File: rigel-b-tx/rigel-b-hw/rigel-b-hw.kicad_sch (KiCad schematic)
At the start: 42 parts, among them IC1 BALFHB-WL-02D3, J1 Conn_01x03_Pin, J3 Conn_01x03_Pin, U1 STM32WLE5C8Ux, U2 XC6206P332MR, U3 CH340X, U4 TYPE-C_16PIN_2MD(073), U5 X1G004131004200, U6 KH-SMA-K513-G

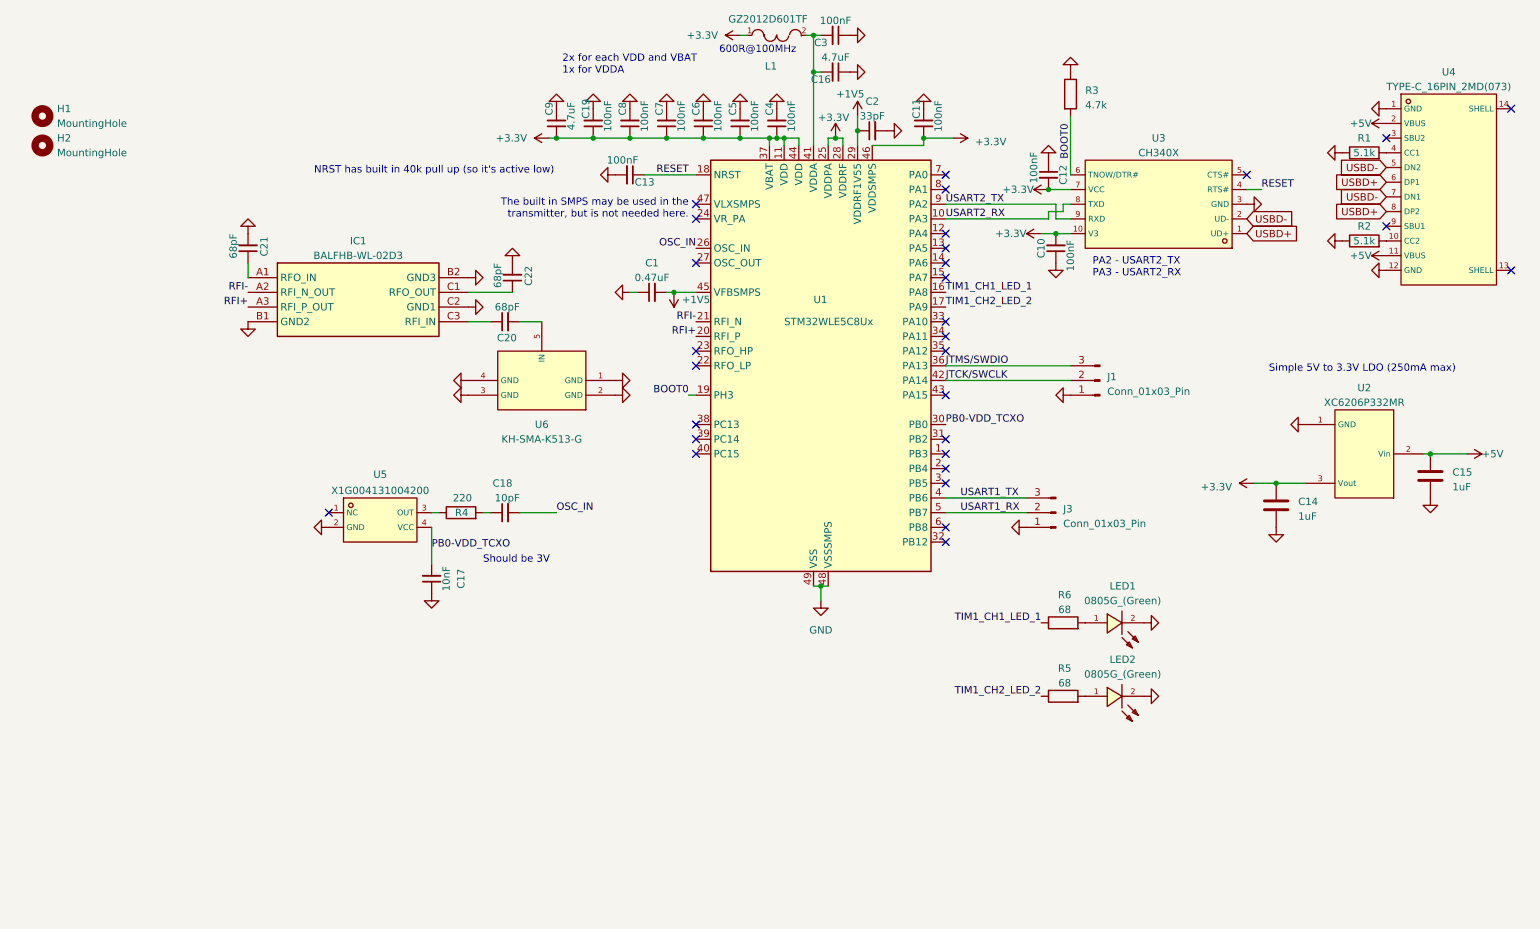
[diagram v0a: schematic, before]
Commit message: Added part of new buck converter
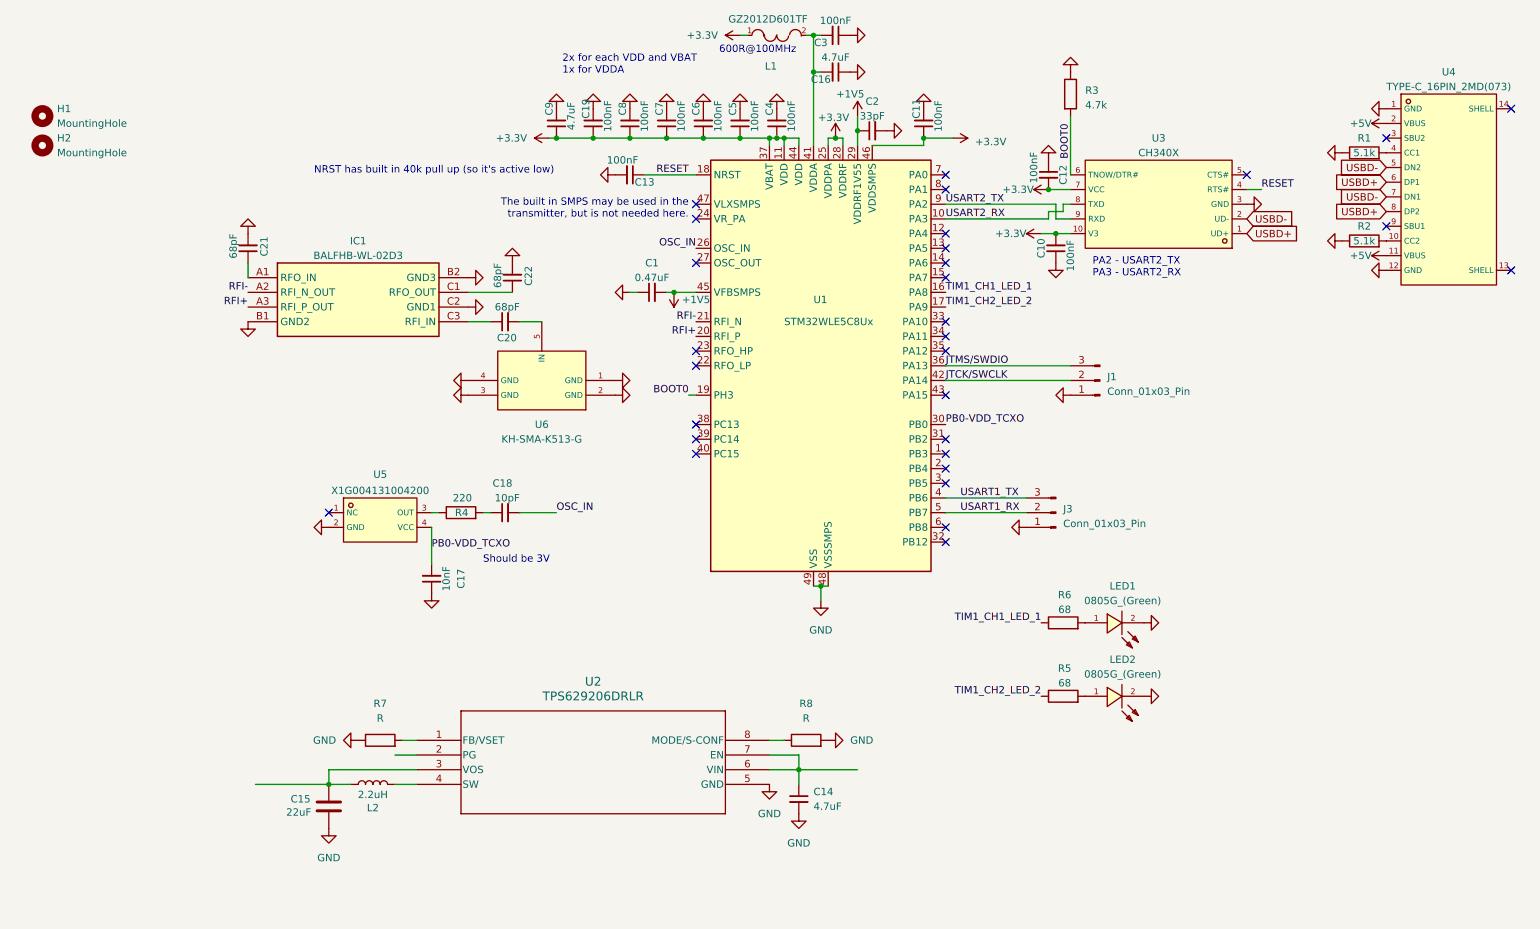
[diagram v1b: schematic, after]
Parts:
- removed C14: 1uF, Capacitor_SMD:C_0603_1608Metric, symbol Device:C
- removed U2: XC6206P332MR, jlc:SOT-23-3_L2.9-W1.6-P1.90-LS2.8-BR, symbol default_lib:XC6206P332MR
- added C14: 4.7uF, symbol Device:C_Small
- added L2: 2.2uH, symbol Device:L
- added R7, R8: R, symbol Device:R
- added U2: TPS629206DRLR, SOT5X3-8_DRL_TEX, symbol 2024-10-27_20-25-40:TPS629206DRLR
- C15: value 1uF -> 22uF; footprint Capacitor_SMD:C_0603_1608Metric -> (none)
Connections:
- net +5V: no longer C15.1
- net GND: now also C15.1, C14.2, R7.1, R8.2, U2.5 (GND); no longer C15.2
- new net: R7.2, U2.1 (FB/VSET)
- new net: C15.2, L2.1, U2.3 (VOS)
- new net: L2.2, U2.4 (SW)
- new net: C14.1, U2.6 (VIN), U2.7 (EN)
- new net: R8.1, U2.8 (MODE/S-CONF)
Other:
- note removed: "Simple 5V to 3.3V LDO (250mA max)"

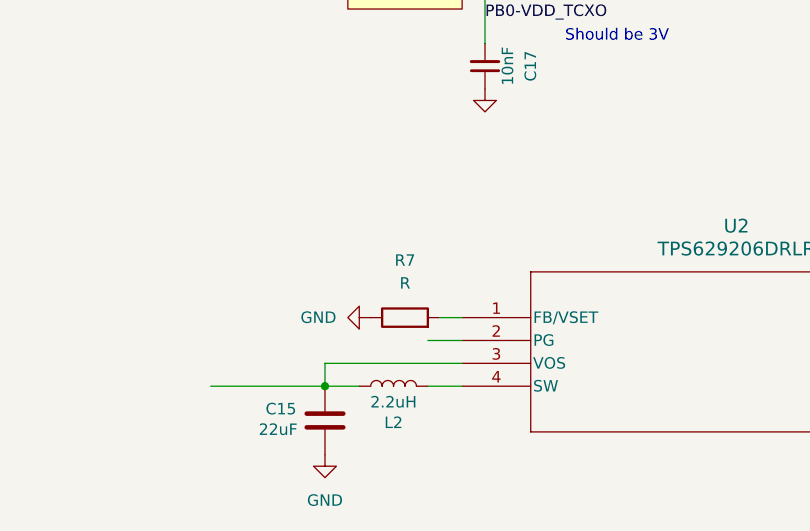
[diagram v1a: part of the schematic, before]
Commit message: Update resistor value
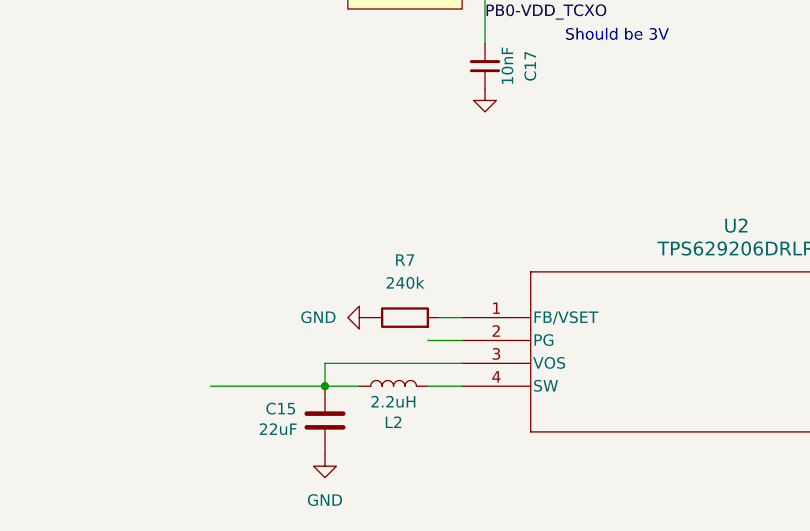
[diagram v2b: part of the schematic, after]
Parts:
- R7: value R -> 240k
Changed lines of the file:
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@@
 			)
 		)
-		(property "Value" "R"
+		(property "Value" "240k"
 			(at 83.82 134.62 90)
 			(effects

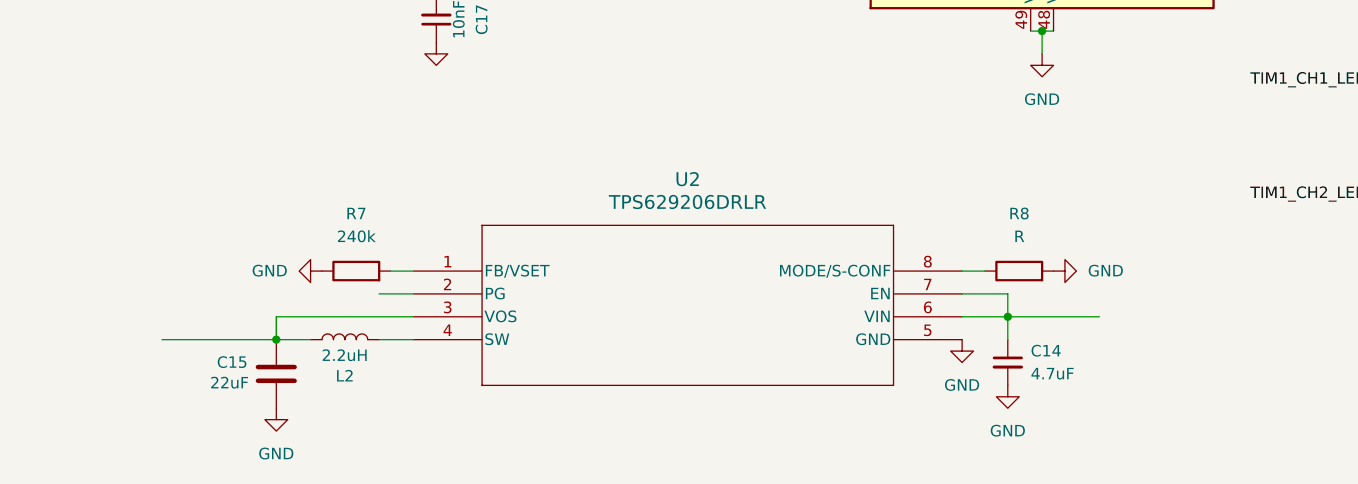
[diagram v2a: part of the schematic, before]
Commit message: Finish buck converter
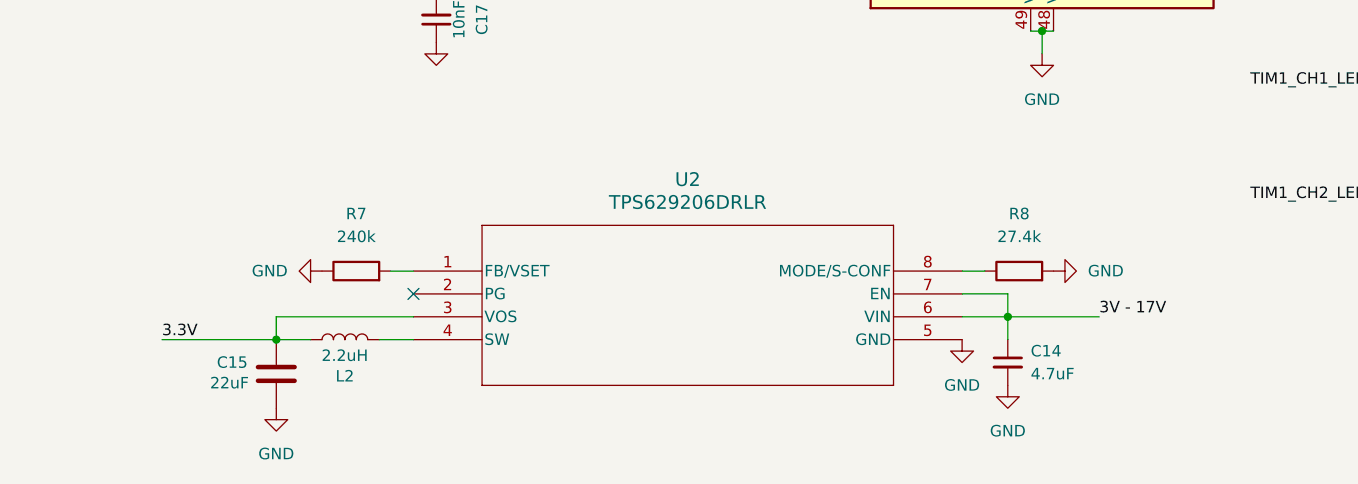
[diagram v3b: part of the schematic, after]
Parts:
- R8: value R -> 27.4k
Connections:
- net 3.3V: now reaches C15.2, L2.1, U2.3 (VOS)
- net 3V - 17V: now reaches C14.1, U2.6 (VIN), U2.7 (EN)
- no-connect marks 30 -> 31
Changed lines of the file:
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@@
+	)
+	(no_connect
+		(at 90.17 140.97)
 	)
 	(no_connect
@@
 		(pts
 			(xy 160.02 22.86) (xy 158.75 22.86)
-		)
-		(stroke
-			(width 0)
-			(type default)
-		)
-	)
-	(wire
-		(pts
-			(xy 86.36 140.97) (xy 90.17 140.97)
 		)
 		(stroke
@@
 		)
 	)
+	(label "3.3V"
+		(at 62.23 146.05 0)
+		(fields_autoplaced yes)
+		(effects
+			(font
+				(size 1.27 1.27)
+			)
+			(justify left bottom)
+		)
+	)
 	(label "JTCK{slash}SWCLK"
 		(at 181.61 76.2 0)
@@
 	(label "USART1_RX"
 		(at 184.15 99.06 0)
+		(fields_autoplaced yes)
+		(effects
+			(font
+				(size 1.27 1.27)
+			)
+			(justify left bottom)
+		)
+	)
+	(label "3V - 17V"
+		(at 166.37 143.51 0)
 		(fields_autoplaced yes)
 		(effects
@@
 			)
 		)
-		(property "Value" "R"
+		(property "Value" "27.4k"
 			(at 157.48 134.62 90)
 			(effects

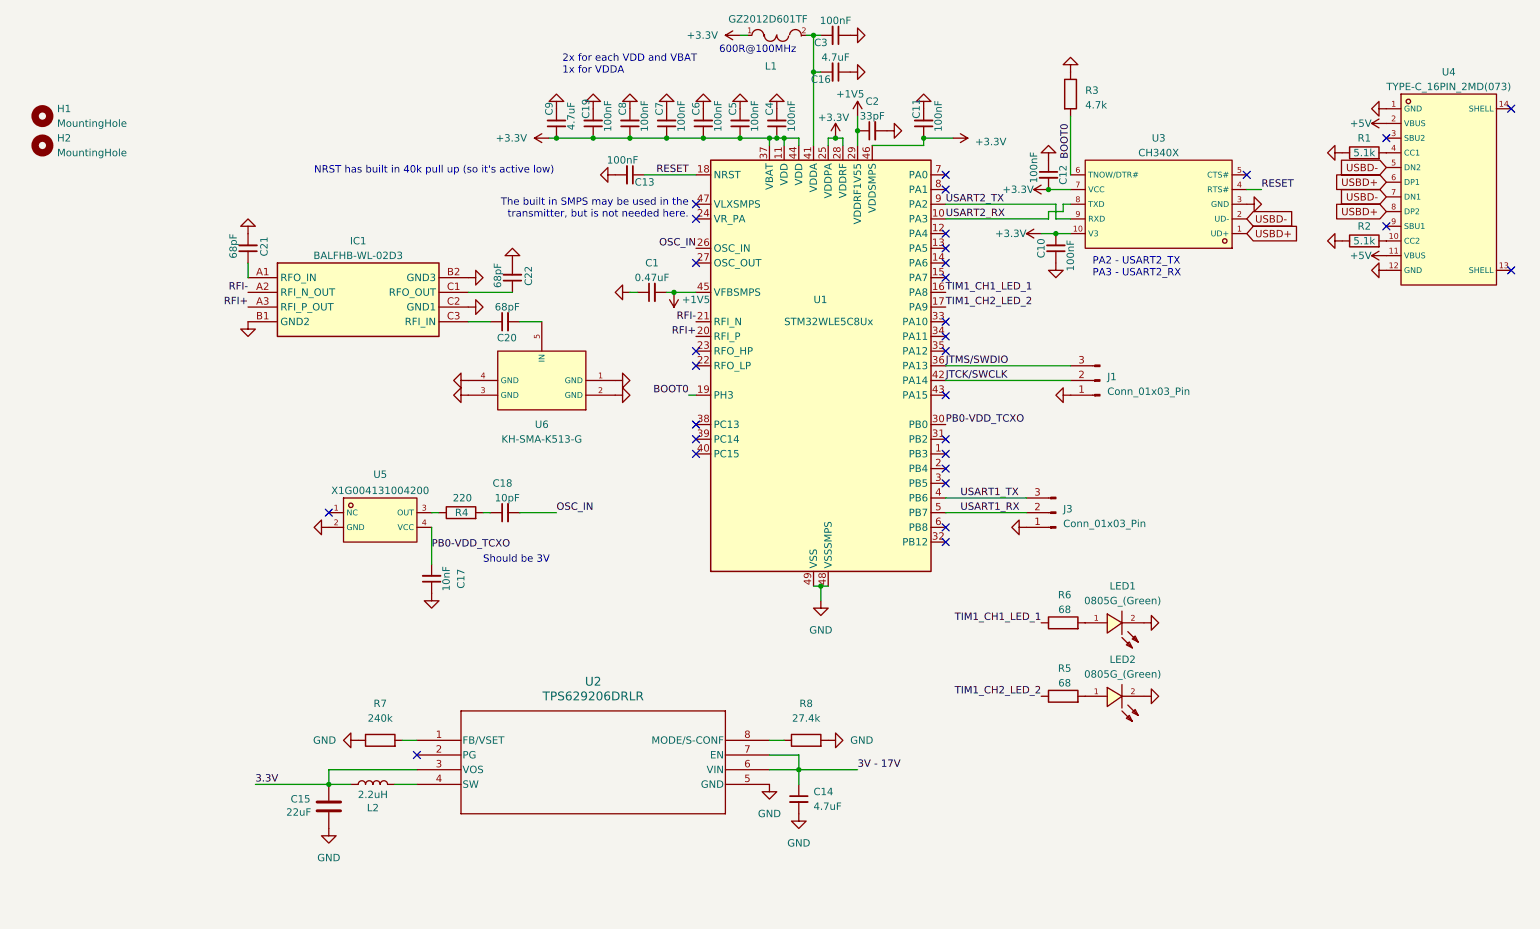
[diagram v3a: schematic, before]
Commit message: Buck converter + power switch
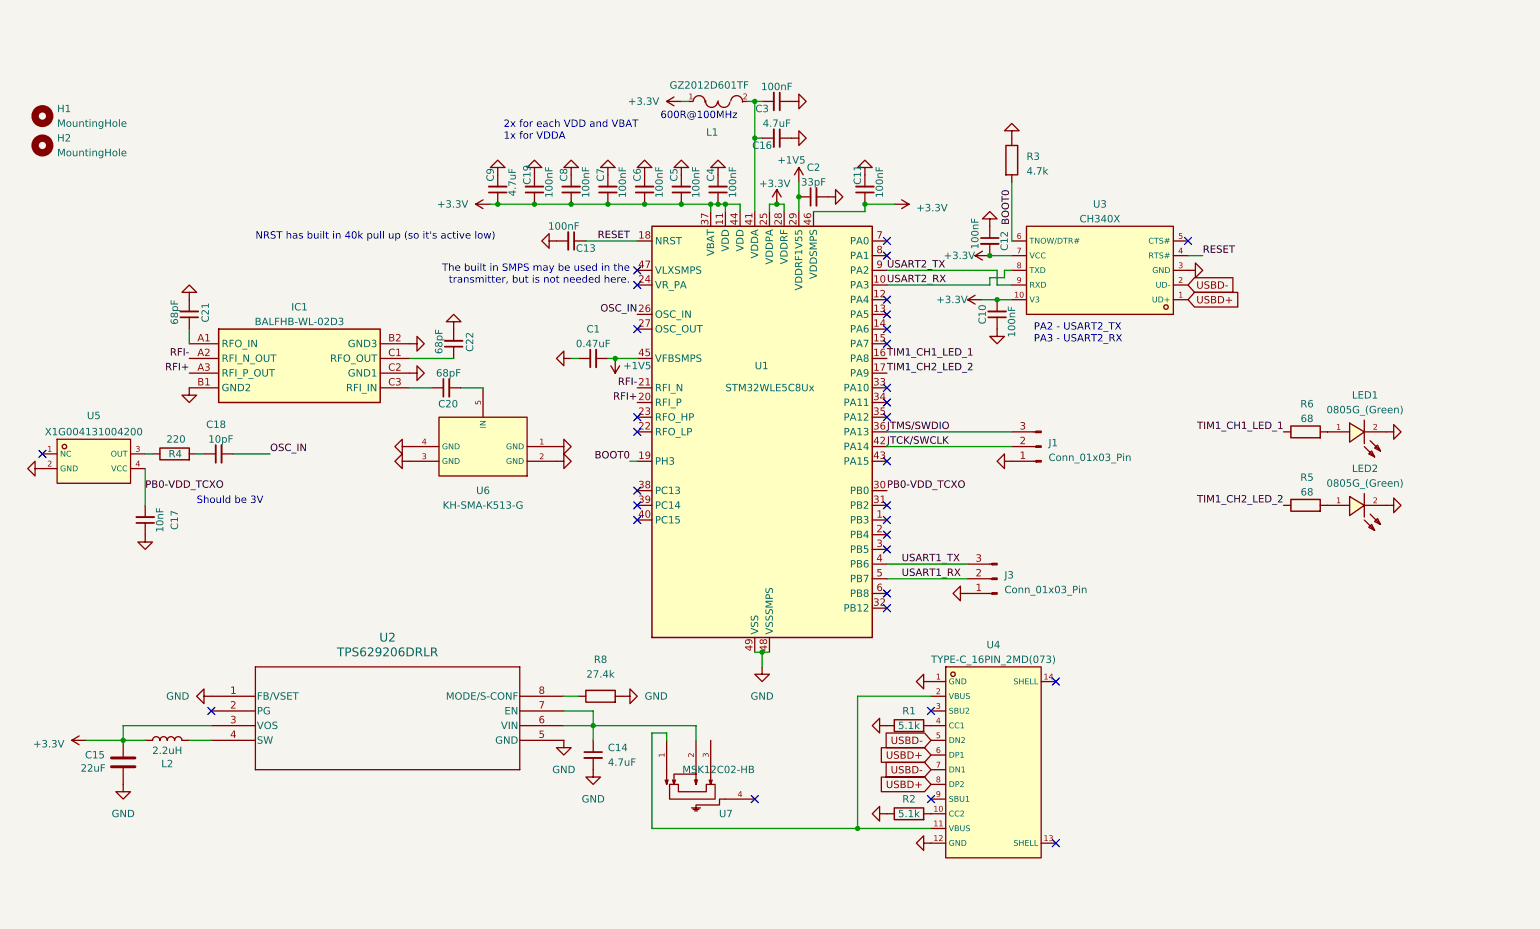
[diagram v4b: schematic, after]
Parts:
- removed R7: 240k, symbol Device:R
- added U7: MSK12C02-HB, jlc:SW-TH_MSK12C02-HB-1, symbol polaris-sym:MSK12C02-HB
- C14, C15: footprint (none) -> Capacitor_SMD:C_0603_1608Metric
- L2: footprint (none) -> Inductor_SMD:L_0603_1608Metric
- R8: footprint (none) -> Resistor_SMD:R_0402_1005Metric
- U2: footprint SOT5X3-8_DRL_TEX -> jlc:SOT5X3-8_DRL_TEX
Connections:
- net 3.3V is gone; now on net +3.3V: C15.2, L2.1, U2.3 (VOS)
- net GND: now also U2.1 (FB/VSET)
- net +5V: no longer names the net of U4.11 (VBUS), U4.2 (VBUS)
- net +5V: now also U7.1
- net 3V - 17V: no longer names the net of C14.1, U2.6 (VIN), U2.7 (EN)
- net 3V - 17V: now also U7.2
- no-connect marks 31 -> 32
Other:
- moved on the sheet: C1, C10, C11, C12, C13, C14, C15, C16, C17, C18, C19, C2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

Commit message: Battery connector
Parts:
- added J2: 436500200, CON_436500200_MOL, symbol 2024-11-03_22-45-00:436500200
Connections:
- net GND: now also J2.2
- net at U7.3: now also J2.1
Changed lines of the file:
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@@
 	(wire
 		(pts
+			(xy 140.97 138.43) (xy 157.48 138.43)
+		)
+		(stroke
+			(width 0)
+			(type default)
+		)
+	)
+	(wire
+		(pts
+			(xy 157.48 138.43) (xy 157.48 160.02)
+		)
+		(stroke
+			(width 0)
+			(type default)
+		)
+	)
+	(wire
+		(pts
 			(xy 143.51 45.72) (xy 143.51 46.99)
 		)
@@
 	)
 	(symbol
+		(lib_id "2024-11-03_22-45-00:436500200")
+		(at 157.48 160.02 0)
+		(unit 1)
+		(exclude_from_sim no)
+		(in_bom yes)
+		(on_board yes)
+		(dnp no)
+		(fields_autoplaced yes)
+		(property "Reference" "J2"
+			(at 171.45 160.0199 0)
+			(effects
+				(font
+					(size 1.524 1.524)
+				)
+				(justify left)
+			)
+		)
+		(property "Value" "436500200"
+			(at 171.45 162.5599 0)
+			(effects
+				(font
+					(size 1.524 1.524)
+				)
+				(justify left)
+			)
+		)
+		(property "Footprint" "CON_436500200_MOL"
+			(at 157.48 160.02 0)
+			(effects
+				(font
+					(size 1.27 1.27)
+					(italic yes)
+				)
+				(hide yes)
+			)
+		)
+		(property "Datasheet" "436500200"
+			(at 157.48 160.02 0)
+			(effects
+				(font
+					(size 1.27 1.27)
+					(italic yes)
+				)
+				(hide yes)
+			)
+		)
+		(property "Description" ""
+			(at 157.48 160.02 0)
+			(effects
+				(font
+					(size 1.27 1.27)
+				)
+				(hide yes)
+			)
+		)
+		(pin "1"
+		)
+		(pin "2"
+		)
+		(instances
+			(project ""
+				(path "/5b772f1b-b884-4184-9180-5f1d0867ded9"
+					(reference "J2")
+					(unit 1)
+				)
+			)
+		)
+	)
+	(symbol
 		(lib_id "power:GND")
 		(at 114.3 87.63 90)
@@
 					(unit 1)
 				)
+			)
+		)
+	)
+	(symbol
+		(lib_name "GND_6")
+		(lib_id "power:GND")
+		(at 157.48 162.56 0)
+		(unit 1)
+		(exclude_from_sim no)
+		(in_bom yes)
+		(on_board yes)
+		(dnp no)
+		(fields_autoplaced yes)
+		(property "Reference" "#PWR019"
+			(at 157.48 168.91 0)
+			(effects
+				(font
+					(size 1.27 1.27)
+				)
+				(hide yes)
+			)
+		)
+		(property "Value" "GND"
+			(at 157.48 167.64 0)
+			(effects
+				(font
+					(size 1.27 1.27)
+				)
+			)
+		)
+		(property "Footprint" ""
+			(at 157.48 162.56 0)
+			(effects
+				(font
+					(size 1.27 1.27)
+				)
+				(hide yes)
+			)
+		)
+		(property "Datasheet" ""
+			(at 157.48 162.56 0)
+			(effects
+				(font
+					(size 1.27 1.27)
+				)
+				(hide yes)
+			)
+		)
+		(property "Description" "Power symbol creates a global label with name \"GND\" , ground"
+			(at 157.48 162.56 0)
+			(effects
+				(font
+					(size 1.27 1.27)
+				)
+				(hide yes)
+			)
+		)
+		(pin "1"
+		)
+		(instances
+			(project ""
+				(path "/5b772f1b-b884-4184-9180-5f1d0867ded9"
+					(reference "#PWR019")
+					(unit 1)
+				)

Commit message: Diodes
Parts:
- added CR1, CR2: VS-E7FX0112HM3/I, CR_SMF_DO-219AB_VIS, symbol 2024-11-05_21-21-38:VS-E7FX0112HM3_I
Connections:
- net +3.3V: no longer C15.2, L2.1, U2.3 (VOS)
- net GND: now also J2.1; no longer J2.2
- net at U4.11 (VBUS), U4.2 (VBUS): now also U7.3; no longer U7.1
- new net: C15.2, CR1.2, L2.1, U2.3 (VOS)
- new net: J2.2, U7.1
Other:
- moved on the sheet: C14, C15, J2, L2, R1, R2, U4, U7
